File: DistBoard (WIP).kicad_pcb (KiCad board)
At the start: 2 copper layers, 83.8 x 73.7 mm, 51 parts, among them J1 22-27-2021, J10 Conn_01x03, J11 Conn_01x03, J12 Conn_01x03, J13 Conn_01x03, J14 PPTC241LFBN-RC, J15 PPTC241LFBN-RC, J2 Conn_01x03, J3 Conn_01x03, J4 Conn_01x03, J5 Conn_01x03, J6 Conn_01x03, J7 Conn_01x03, J8 Conn_01x03, J9 Conn_01x03, U1 TLE2426CDR

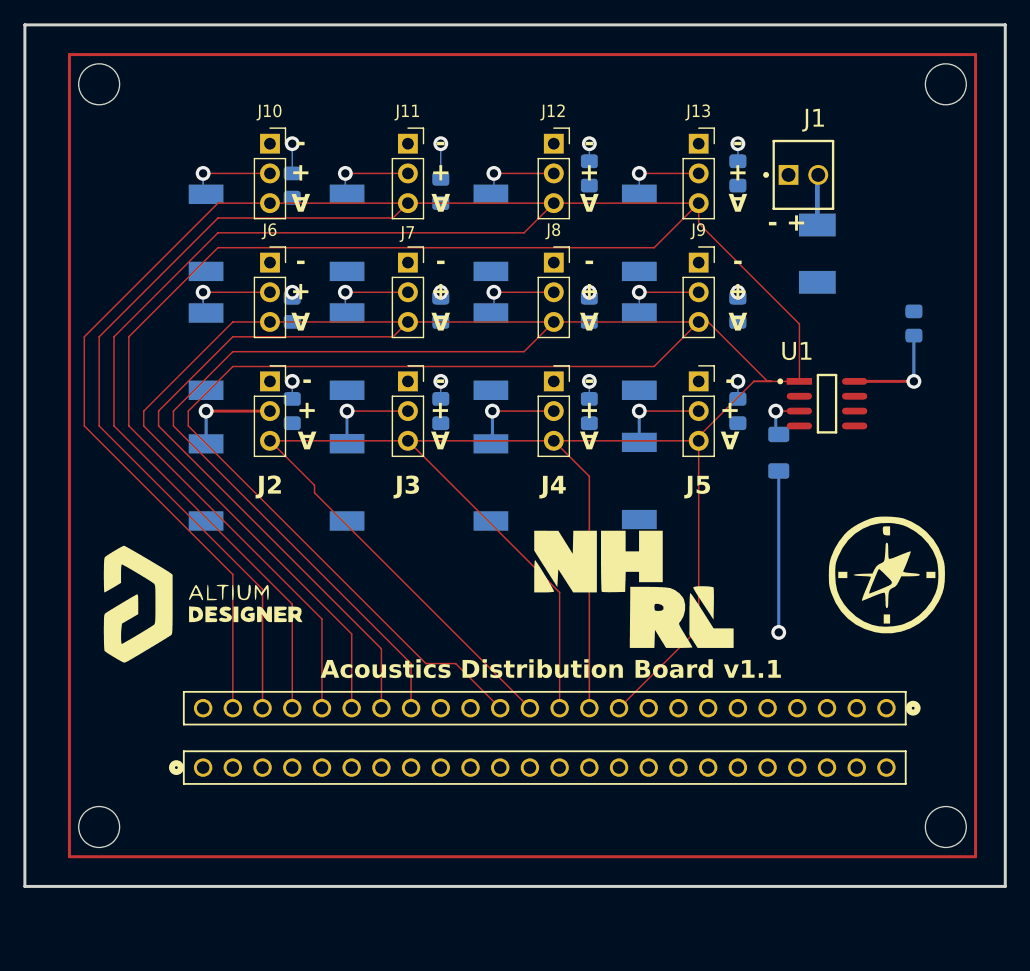
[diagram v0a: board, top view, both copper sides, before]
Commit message: Changed PCB to correct spacing on all headers and corrected routes to FPGA headers. Changed schematic to include net labels instead of physical wires and corrected routing from single channel boards to FPGA headers.
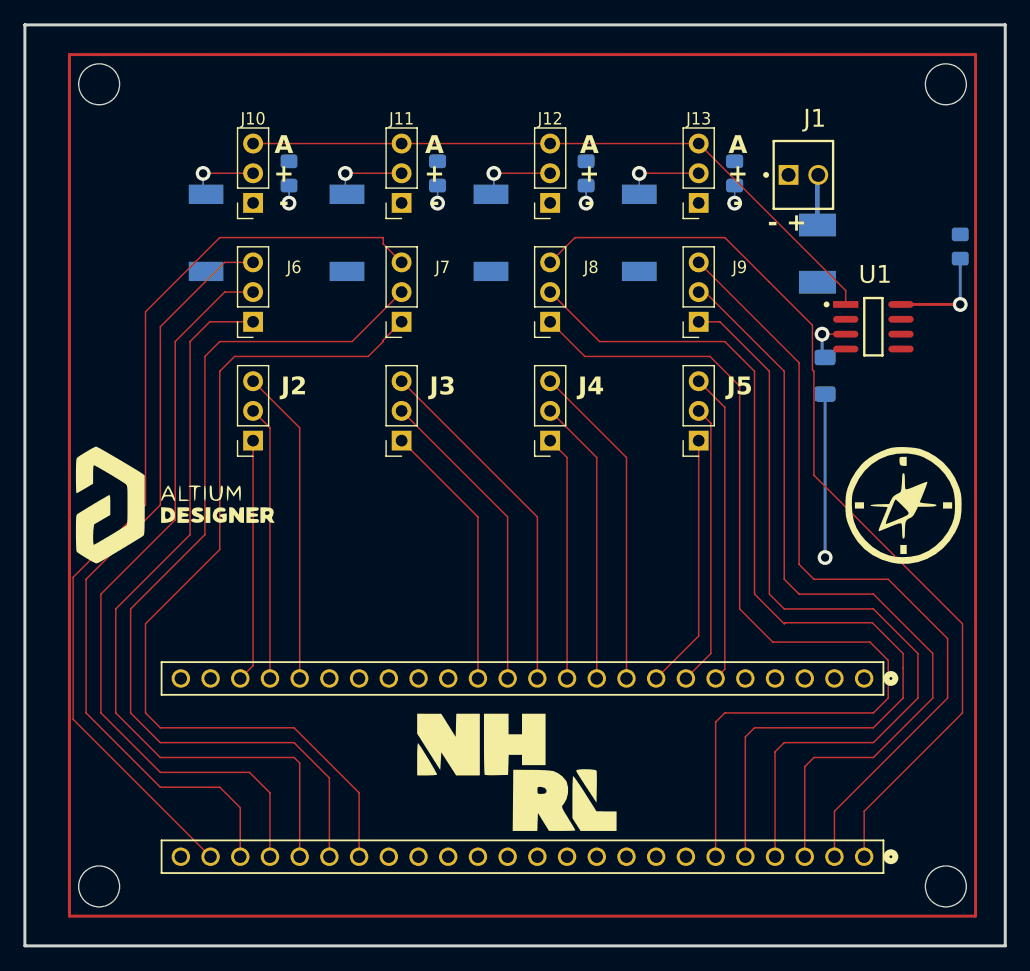
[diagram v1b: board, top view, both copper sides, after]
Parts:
- removed C1, C10, C2, C3, C4, C7, C8, C9: 1uF, Capacitor_SMD:C_0805_2012Metric_Pad1.18x1.45mm_HandSolder
- removed F2, F3, F4, F5, F6, F7, F8, F9: 0.25A, AltiumImport:LFUS-459_V
- moved J15 57.0 mm to (175.7, 143.1), turned to 180 degrees
- moved G*** 18.6 mm to (146.1, 135.9)
- moved G*** 8.81 mm to (116.8, 113.0)
- moved C5 7.68 mm to (184.0, 90.9)
- moved U1 7.68 mm to (176.5, 97.8)
- moved C6 7.68 mm to (172.4, 102.0)
- moved G*** 6.11 mm to (179.1, 113.0)
- moved J10 5.27 mm to (123.5, 87.2), turned to 180 degrees
- moved J6 5.27 mm to (123.5, 97.4), turned to 180 degrees
- moved J2 5.27 mm to (123.5, 107.5), turned to 180 degrees
- moved J11 5.09 mm to (136.2, 87.2), turned to 180 degrees
- moved J7 5.09 mm to (136.2, 97.4), turned to 180 degrees
- moved J3 5.09 mm to (136.2, 107.5), turned to 180 degrees
- moved ? 5.08 mm to (182.7, 145.6)
- moved ? 5.08 mm to (110.3, 145.6)
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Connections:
- C11 pad 2: /VCC -> +5V
- C12 pad 2: /VCC -> +5V
- C13 pad 2: /VCC -> +5V
- C14 pad 2: /VCC -> +5V
- C5 pad 2: /VCC -> +5V
- C6 pad 1: /VCC -> +5V
- F1 pad 2: /VCC -> +5V
- F10 pad 1: /VCC -> +5V
- F11 pad 1: /VCC -> +5V
- F12 pad 1: /VCC -> +5V
- F13 pad 1: /VCC -> +5V
- J14 pad 10: /AGND -> /J4 (CLK)
- J14 pad 11: /AGND -> /J4 (DOUT)
- J14 pad 12: /AGND -> /J3 (CS)
- J14 pad 13: /AGND -> /J3 (CLK)
- J14 pad 14: /AGND -> /J3 (DOUT)
- J14 pad 17: /AGND -> unconnected-(J14-Pad17)
- J14 pad 18: /AGND -> unconnected-(J14-Pad18)
- J14 pad 19: /AGND -> unconnected-(J14-Pad19)
- J14 pad 20: /AGND -> /J2 (CS)
- J14 pad 21: /AGND -> /J2 (CLK)
- J14 pad 22: /AGND -> /J2 (DOUT)
- J14 pad 23: /AGND -> unconnected-(J14-Pad23)
- J14 pad 24: /VCC -> unconnected-(J14-Pad24)
- J14 pad 6: unconnected-(J14-Pad6) -> /J5 (CS)
- J14 pad 7: unconnected-(J14-Pad7) -> /J5 (CLK)
- J14 pad 8: unconnected-(J14-Pad8) -> /J5 (DOUT)
- J14 pad 9: unconnected-(J14-Pad9) -> /J4 (CS)
- J15 pad 1: GND -> /J8 (G2 OUT)
- J15 pad 18: unconnected-(J15-Pad18) -> /J7 (G0 OUT)
- J15 pad 19: unconnected-(J15-Pad19) -> /J7 (G1 OUT)
- J15 pad 2: Net-(J3-Pin_3) -> /J9 (G2 OUT)
- J15 pad 20: unconnected-(J15-Pad20) -> /J6 (G0 OUT)
- J15 pad 21: unconnected-(J15-Pad21) -> /J6 (G1 OUT)
- J15 pad 22: unconnected-(J15-Pad22) -> /J6 (G2 OUT)
- J15 pad 23: unconnected-(J15-Pad23) -> /J7 (G2 OUT)
- J15 pad 24: unconnected-(J15-Pad24) -> GND
- J15 pad 3: Net-(J7-Pin_3) -> /J9 (G1 OUT)
- J15 pad 4: Net-(J11-Pin_3) -> /J9 (G0 OUT)
- J15 pad 5: Net-(J2-Pin_3) -> /J8 (G1 OUT)
- J15 pad 6: Net-(J6-Pin_3) -> /J8 (G0 OUT)
- J15 pad 7: Net-(J10-Pin_3) -> unconnected-(J15-Pad7)
- J2 pad 1: GND -> /J2 (DOUT)
- J2 pad 2: Net-(J2-Pin_2) -> /J2 (CLK)
- J2 pad 3: /AGND -> /J2 (CS)
- J3 pad 1: GND -> /J3 (DOUT)
- J3 pad 2: Net-(J3-Pin_2) -> /J3 (CLK)
- J3 pad 3: /AGND -> /J3 (CS)
- J4 pad 1: GND -> /J4 (DOUT)
- J4 pad 2: Net-(J4-Pin_2) -> /J4 (CLK)
- J4 pad 3: /AGND -> /J4 (CS)
- J5 pad 1: GND -> /J5 (DOUT)
- J5 pad 2: Net-(J5-Pin_2) -> /J5 (CLK)
- J5 pad 3: /AGND -> /J5 (CS)
- J6 pad 1: GND -> /J6 (G0 OUT)
- J6 pad 2: Net-(J6-Pin_2) -> /J6 (G1 OUT)
- J6 pad 3: /AGND -> /J6 (G2 OUT)
- J7 pad 1: GND -> /J7 (G0 OUT)
- J7 pad 2: Net-(J7-Pin_2) -> /J7 (G1 OUT)
- J7 pad 3: /AGND -> /J7 (G2 OUT)
- J8 pad 1: GND -> /J8 (G0 OUT)
- J8 pad 2: Net-(J8-Pin_2) -> /J8 (G1 OUT)
- J8 pad 3: /AGND -> /J8 (G2 OUT)
- J9 pad 1: GND -> /J9 (G0 OUT)
- J9 pad 2: Net-(J9-Pin_2) -> /J9 (G1 OUT)
- J9 pad 3: /AGND -> /J9 (G2 OUT)
- U1 pad 3: /VCC -> +5V
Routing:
- net /AGND: track 818.2 -> 57.1 mm
- net /J8 (G1 OUT): track 0.00 -> 83.1 mm
- net /J8 (G0 OUT): track 0.00 -> 82.4 mm
- net /J8 (G2 OUT): track 0.00 -> 80.6 mm
- net /J7 (G2 OUT): track 0.00 -> 79.7 mm
- net /J7 (G1 OUT): track 0.00 -> 78.2 mm
- net /J7 (G0 OUT): track 0.00 -> 75.8 mm
- net /J9 (G0 OUT): track 0.00 -> 69.4 mm
- net /J9 (G1 OUT): track 0.00 -> 68.1 mm
- net /J9 (G2 OUT): track 0.00 -> 67.4 mm
- net /J6 (G2 OUT): track 0.00 -> 66.6 mm
- net /J6 (G0 OUT): track 0.00 -> 66.0 mm
- net /J6 (G1 OUT): track 0.00 -> 65.5 mm
- net /J3 (CS): track 0.00 -> 30.2 mm
- net /J4 (CS): track 0.00 -> 28.1 mm
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- added copper zone on B.Cu, net +5V
- removed copper zone on B.Cu, net /VCC
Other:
- board size 83.8 x 73.7 mm -> 83.8 x 78.7 mm
- board text added: "Acoustics Distribution Board v2.0"
- board text removed: "Acoustics Distribution Board v1.1"
